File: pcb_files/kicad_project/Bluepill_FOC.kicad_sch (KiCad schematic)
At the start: 27 parts, among them IC1 AS5145B-HSST, J1 Conn_01x03_Pin, J2 Conn_01x03_Pin, SW1 SW_Reset, U4 BluePill, Y2 Crystal

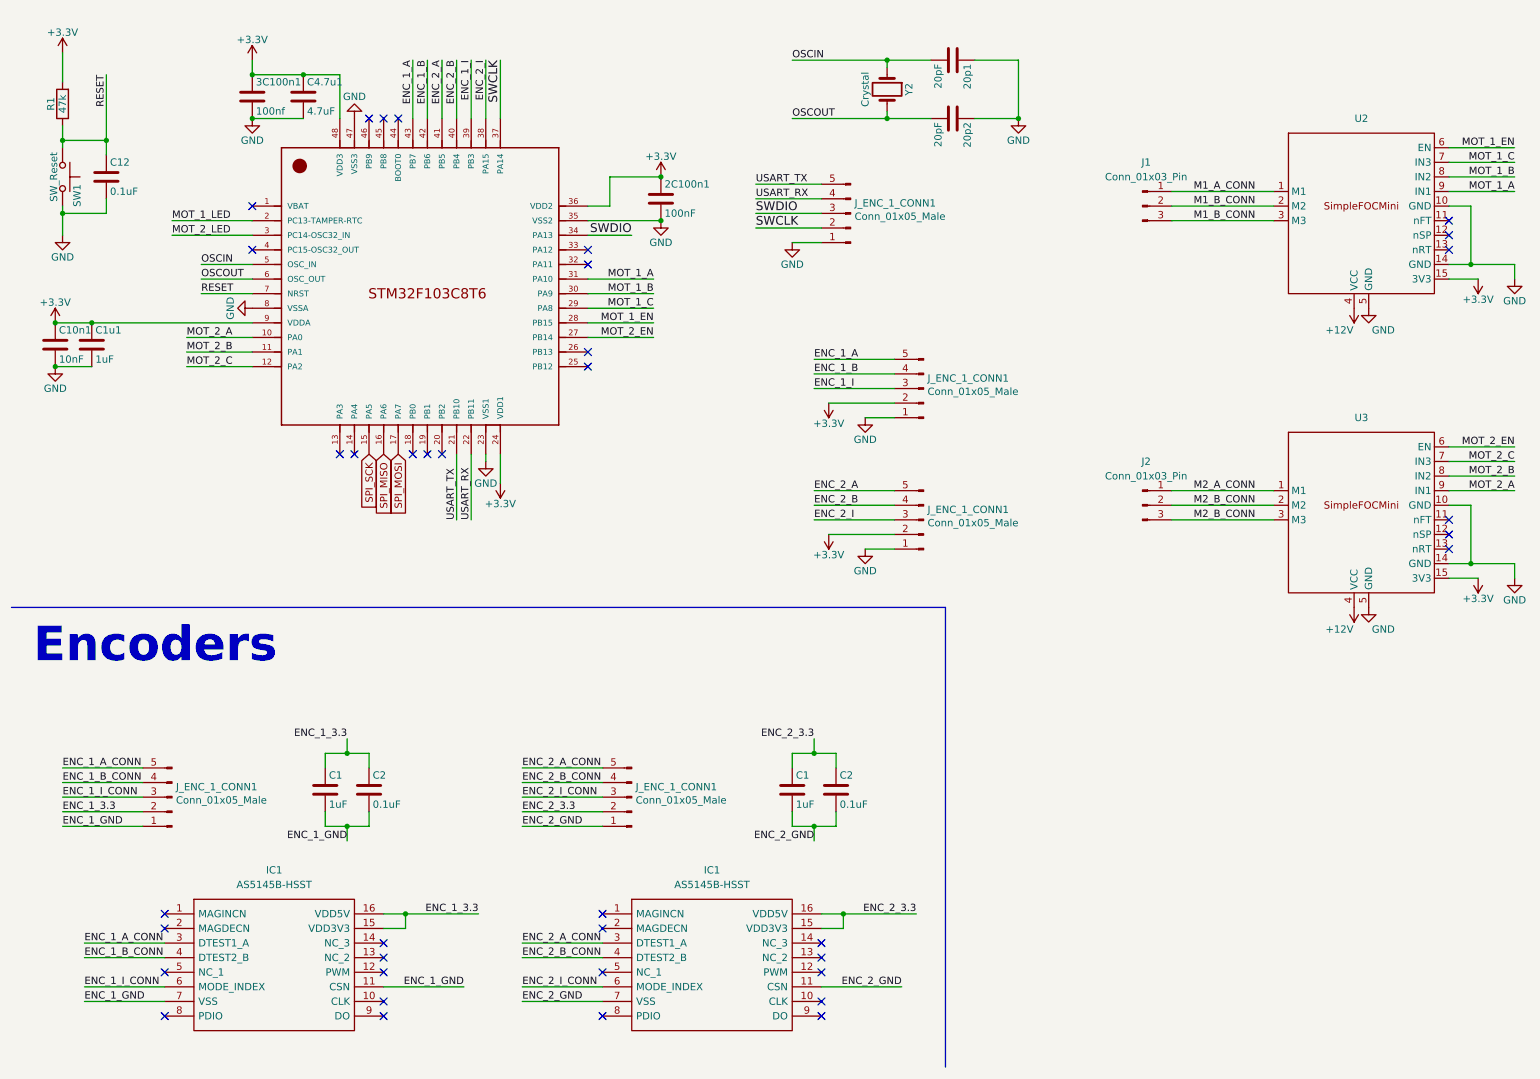
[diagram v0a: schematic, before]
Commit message: Añade pinout de BlackPill, completa esquemático y asocia footprints
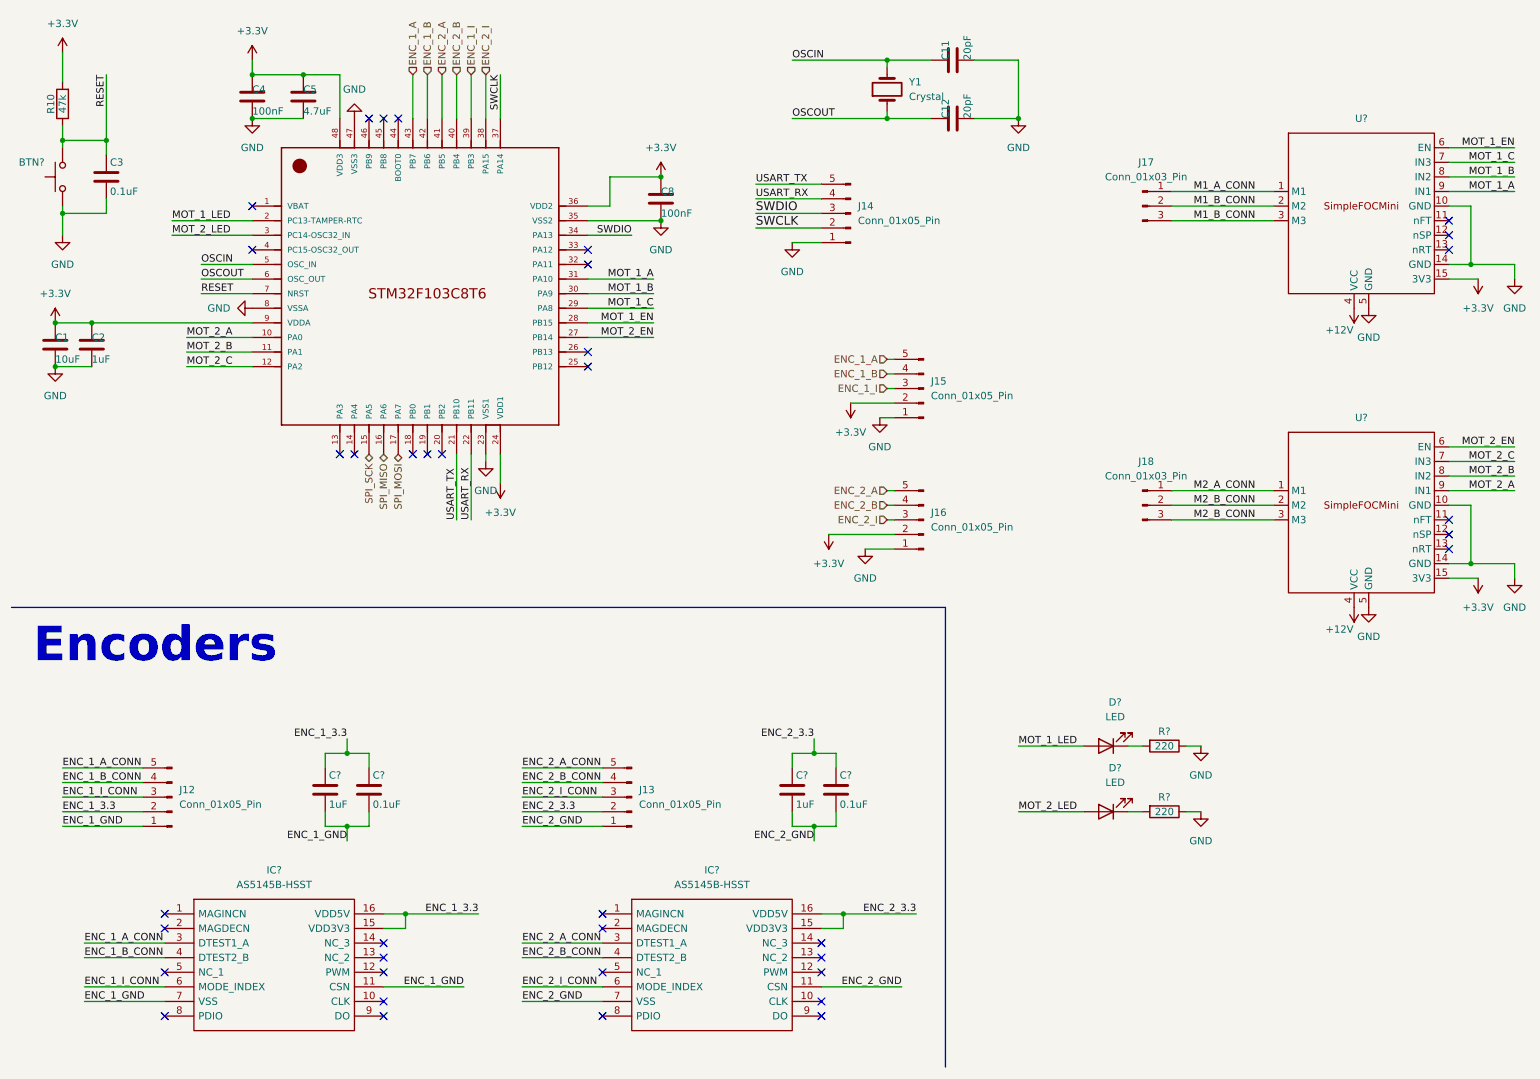
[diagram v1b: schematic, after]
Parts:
- removed 20p1, 20p2: 20pF, Capacitors_SMD:C_0805, symbol DragonBot-rescue:C
- removed 2C100n1: 100nF, Capacitors_SMD:C_0805, symbol DragonBot-rescue:C
- removed 3C100n1: 100nf, Capacitors_SMD:C_0805, symbol DragonBot-rescue:C
- removed C10n1: 10nF, Capacitors_SMD:C_0805, symbol DragonBot-rescue:C
- removed C1u1: 1uF, Capacitors_SMD:C_0805, symbol DragonBot-rescue:C
- removed C4.7u1: 4.7uF, Capacitors_SMD:C_0805, symbol DragonBot-rescue:C
- removed J_ENC_1_CONN1 (x5): Conn_01x05_Male, PCB_ZoroBot_v3:encd_fuji, symbol PCB_ZoroBot_v3-rescue:Conn_01x05_Male-Connector
- removed SW1: SW_Reset, Button_Switch_SMD:SW_SPST_EVQPE1, symbol PCB_ZoroBot_v3-rescue:SW_Push-multiPCB-rescue-multiPCB-rescue-PCB_Fujitora-resc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
- removed Y2: Crystal, Crystals:Crystal_HC50_Vertical, symbol DragonBot-rescue:Crystal
- added BTN?: ~, Button_Switch_SMD:SW_SPST_EVQPE1, symbol custom_libraries:Button
- added C1: 10uF, Capacitor_SMD:C_0805_2012Metric, symbol Device:C
- added C11, C12: 20pF, Capacitor_SMD:C_0805_2012Metric, symbol Device:C
- added C2: 1uF, Capacitor_SMD:C_0805_2012Metric, symbol Device:C
- added C4, C8: 100nF, Capacitor_SMD:C_0805_2012Metric, symbol Device:C
- added C5: 4.7uF, Capacitor_SMD:C_0805_2012Metric, symbol Device:C
- added D? (x2): LED, LED_SMD:LED_0805_2012Metric, symbol Device:LED
- added J12, J13, J14, J15, J16: Conn_01x05_Pin, Connector_PinHeader_2.54mm:PinHeader_1x05_P2.54mm_Vertical, symbol Connector:Conn_01x05_Pin
- added R? (x2): 220, Resistor_SMD:R_0805_2012Metric_Pad1.20x1.40mm_HandSolder, symbol Device:R
- added Y1: Crystal, Crystal:Crystal_SMD_5032-2Pin_5.0x3.2mm, symbol Device:Crystal
- IC? (x2): renamed from IC1; footprint (none) -> Package_SO:SSOP-16_5.3x6.2mm_P0.65mm
- J17: renamed from J1; footprint (none) -> Connector_PinHeader_2.54mm:PinHeader_1x03_P2.54mm_Vertical
- J18: renamed from J2; footprint (none) -> Connector_PinHeader_2.54mm:PinHeader_1x03_P2.54mm_Vertical
- U?: renamed from U4; footprint (none) -> Package_QFP:LQFP-48_7x7mm_P0.5mm
- U?: renamed from U2; footprint (none) -> custom_library:SimpleFOCMini
- U?: renamed from U3; footprint (none) -> custom_library:SimpleFOCMini
- renumbered C12 to C3, C2 to C?, C1 to C?, R1 to R10
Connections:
- net ENC_1_3.3: now also J12.2 (Pin_2)
- net ENC_1_A: now also J15.5 (Pin_5)
- net ENC_1_A_CONN: now also J12.5 (Pin_5)
- net ENC_1_B: now also J15.4 (Pin_4)
- net ENC_1_B_CONN: now also J12.4 (Pin_4)
- net ENC_1_GND: now also J12.1 (Pin_1)
- net ENC_1_I: now also J15.3 (Pin_3)
- net ENC_1_I_CONN: now also J12.3 (Pin_3)
- net ENC_2_3.3: now also J13.2 (Pin_2)
- net ENC_2_A: now also J16.5 (Pin_5)
- net ENC_2_A_CONN: now also J13.5 (Pin_5)
- net ENC_2_B: now also J16.4 (Pin_4)
- net ENC_2_B_CONN: now also J13.4 (Pin_4)
- net ENC_2_GND: now also J13.1 (Pin_1)
- net ENC_2_I: now also J16.3 (Pin_3)
- net ENC_2_I_CONN: now also J13.3 (Pin_3)
- net GND: now also BTN?.1, C1.2, C11.2, C12.2, C2.2, C4.2, C5.2, C8.2, J14.1 (Pin_1), J15.1 (Pin_1), J16.1 (Pin_1), R?.1, R?.1
- net MOT_1_LED: now also D?.2 (A)
- net MOT_2_LED: now also D?.2 (A)
- net OSCIN: now also C11.1, Y1.2
- net OSCOUT: now also C12.1, Y1.1
- net RESET: now also BTN?.2
- net SWCLK: now also J14.2 (Pin_2)
- net SWDIO: now also J14.3 (Pin_3)
- net USART_RX: now also J14.4 (Pin_4)
- net USART_TX: now also J14.5 (Pin_5)
- net +3V3 renamed +3.3V
- net +3.3V: now also C1.1, C2.1, C4.1, C5.1, C8.1, J15.2 (Pin_2), J16.2 (Pin_2)
- new net: D?.1 (K), R?.2 (x2)

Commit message: Actualiza estructura del proyecto (symbols, footprints) y rutas relativas
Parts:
- BTN?: symbol custom_libraries:Button -> custom_symbols:Button
- IC? (x2): symbol custom_libraries:Encoder_AS5145B-HSST -> custom_symbols:Encoder_AS5145B-HSST
- U?: symbol custom_libraries:BluePill -> custom_symbols:BluePill
- U? (x2): footprint custom_library:SimpleFOCMini -> custom_symbols:SimpleFOCMini; symbol custom_libraries:SimpleFOCMini -> custom_symbols:SimpleFOCMini
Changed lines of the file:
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@@
     )
   )
-  (symbol (lib_id "custom_libraries:BluePill") (at 85.09 63.5 0) (unit 1)
+  (symbol (lib_id "custom_symbols:BluePill") (at 85.09 63.5 0) (unit 1)
     (in_bom yes) (on_board yes) (dnp no) (fields_autoplaced)
     (property "Reference" "U?" (at 106.68 36.83 0)
@@
     )
   )
-  (symbol (lib_id "custom_libraries:SimpleFOCMini") (at 247.65 48.26 0) (unit 1)
+  (symbol (lib_id "custom_symbols:SimpleFOCMini") (at 247.65 48.26 0) (unit 1)
     (in_bom yes) (on_board yes) (dnp no) (fields_autoplaced)
     (property "Reference" "U?" (at 247.65 33.02 0)
@@
       (effects (font (size 1.27 1.27)))
     )
-    (property "Footprint" "custom_library:SimpleFOCMini" (at 247.65 48.26 0)
+    (property "Footprint" "custom_symbols:SimpleFOCMini" (at 247.65 48.26 0)
       (effects (font (size 1.27 1.27)) hide)
     )
@@
     )
   )
-  (symbol (lib_id "custom_libraries:SimpleFOCMini") (at 247.65 100.33 0) (unit 1)
+  (symbol (lib_id "custom_symbols:SimpleFOCMini") (at 247.65 100.33 0) (unit 1)
     (in_bom yes) (on_board yes) (dnp no) (fields_autoplaced)
     (property "Reference" "U?" (at 247.65 85.09 0)
@@
       (effects (font (size 1.27 1.27)))
     )
-    (property "Footprint" "custom_library:SimpleFOCMini" (at 247.65 100.33 0)
+    (property "Footprint" "custom_symbols:SimpleFOCMini" (at 247.65 100.33 0)
       (effects (font (size 1.27 1.27)) hide)
     )
@@
     )
   )
-  (symbol (lib_id "custom_libraries:Button") (at 21.59 43.18 90) (unit 1)
+  (symbol (lib_id "custom_symbols:Button") (at 21.59 43.18 90) (unit 1)
     (in_bom yes) (on_board yes) (dnp no)
     (property "Reference" "BTN?" (at 13.97 40.64 90)
@@
     )
   )
-  (symbol (lib_id "custom_libraries:Encoder_AS5145B-HSST") (at 115.57 171.45 0) (unit 1)
+  (symbol (lib_id "custom_symbols:Encoder_AS5145B-HSST") (at 115.57 171.45 0) (unit 1)
     (in_bom yes) (on_board yes) (dnp no) (fields_autoplaced)
     (property "Reference" "IC?" (at 134.62 163.83 0)
@@
     )
   )
-  (symbol (lib_id "custom_libraries:Encoder_AS5145B-HSST") (at 39.37 171.45 0) (unit 1)
+  (symbol (lib_id "custom_symbols:Encoder_AS5145B-HSST") (at 39.37 171.45 0) (unit 1)
     (in_bom yes) (on_board yes) (dnp no) (fields_autoplaced)
     (property "Reference" "IC?" (at 58.42 163.83 0)

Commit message: Actualiza el esquemático de la PCB
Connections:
- net SPI_NSS: now reaches U?.14 (PA4)
- net USART_RX renamed USART3_RX
- net USART3_RX: now also U?.21 (PB10); no longer U?.22 (PB11)
- net USART_TX renamed USART3_TX
- net USART3_TX: now also U?.22 (PB11); no longer U?.21 (PB10)
- no-connect marks 38 -> 37
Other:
- moved on the sheet: J14
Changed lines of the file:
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@@
   (no_connect (at 54.61 48.26))
   (no_connect (at 262.89 102.87))
-  (no_connect (at 72.39 91.44))
   (no_connect (at 74.93 33.02))
   (no_connect (at 153.67 189.23))
@@
     (stroke (width 0) (type default))
   )
-  (wire (pts (xy 142.24 46.99) (xy 153.67 46.99))
-    (stroke (width 0) (type default))
-  )
   (wire (pts (xy 262.89 38.1) (xy 274.32 38.1))
     (stroke (width 0) (type default))
@@
     (stroke (width 0) (type default))
   )
-  (wire (pts (xy 148.59 54.61) (xy 153.67 54.61))
+  (wire (pts (xy 154.94 57.15) (xy 160.02 57.15))
     (stroke (width 0) (type default))
   )
@@
   )
   (wire (pts (xy 77.47 171.45) (xy 81.28 171.45))
-    (stroke (width 0) (type default))
-  )
-  (wire (pts (xy 90.17 91.44) (xy 90.17 102.87))
     (stroke (width 0) (type default))
   )
@@
     (stroke (width 0) (type default))
   )
-  (wire (pts (xy 142.24 44.45) (xy 153.67 44.45))
-    (stroke (width 0) (type default))
-  )
   (wire (pts (xy 214.63 45.72) (xy 232.41 45.72))
     (stroke (width 0) (type default))
@@
     (stroke (width 0) (type default))
   )
-  (wire (pts (xy 142.24 52.07) (xy 153.67 52.07))
+  (wire (pts (xy 139.7 54.61) (xy 160.02 54.61))
     (stroke (width 0) (type default))
   )
@@
     (stroke (width 0) (type default))
   )
-  (wire (pts (xy 92.71 91.44) (xy 92.71 102.87))
-    (stroke (width 0) (type default))
-  )
   (wire (pts (xy 153.67 173.99) (xy 157.48 173.99))
     (stroke (width 0) (type default))
@@
     (stroke (width 0) (type default))
   )
-  (wire (pts (xy 142.24 49.53) (xy 153.67 49.53))
+  (wire (pts (xy 139.7 52.07) (xy 160.02 52.07))
     (stroke (width 0) (type default))
   )
@@
     (effects (font (size 1.27 1.27)) (justify left bottom))
   )
-  (label "USART_RX" (at 92.71 102.87 90) (fields_autoplaced)
-    (effects (font (size 1.27 1.27)) (justify left bottom))
-  )
   (label "MOT_1_LED" (at 187.96 142.24 0) (fields_autoplaced)
     (effects (font (size 1.27 1.27)) (justify left bottom))
@@
     (effects (font (size 1.27 1.27)) (justify left bottom))
   )
-  (label "USART_TX" (at 142.24 44.45 0) (fields_autoplaced)
-    (effects (font (size 1.27 1.27)) (justify left bottom))
-  )
   (label "OSCOUT" (at 45.72 60.96 0) (fields_autoplaced)
     (effects (font (size 1.27 1.27)) (justify left bottom))
@@
     (effects (font (size 1.27 1.27)) (justify left bottom))
   )
-  (label "USART_TX" (at 90.17 102.87 90) (fields_autoplaced)
-    (effects (font (size 1.27 1.27)) (justify left bottom))
-  )
   (label "SWDIO" (at 120.65 53.34 180) (fields_autoplaced)
     (effects (font (size 1.27 1.27)) (justify right bottom))
@@
     (effects (font (size 1.27 1.27)) (justify left bottom))
   )
-  (label "SWDIO" (at 142.24 49.53 0) (fields_autoplaced)
+  (label "SWDIO" (at 139.7 52.07 0) (fields_autoplaced)
     (effects (font (size 1.524 1.524)) (justify left bottom))
   )
@@
     (effects (font (size 1.27 1.27)) (justify left bottom))
   )
-  (label "SWCLK" (at 142.24 52.07 0) (fields_autoplaced)
+  (label "SWCLK" (at 139.7 54.61 0) (fields_autoplaced)
     (effects (font (size 1.524 1.524)) (justify left bottom))
   )
@@
   (label "SWCLK" (at 97.79 25.4 270) (fields_autoplaced)
     (effects (font (size 1.27 1.27)) (justify right bottom))
-  )
-  (label "USART_RX" (at 142.24 46.99 0) (fields_autoplaced)
-    (effects (font (size 1.27 1.27)) (justify left bottom))
   )
   (label "MOT_1_LED" (at 40.64 50.8 0) (fields_autoplaced)
@@
     (effects (font (size 1.27 1.27)) (justify left))
   )
+  (hierarchical_label "USART3_TX" (shape input) (at 160.02 46.99 180) (fields_autoplaced)
+    (effects (font (size 1.27 1.27)) (justify right))
+  )
+  (hierarchical_label "USART3_TX" (shape input) (at 92.71 91.44 270) (fields_autoplaced)
+    (effects (font (size 1.27 1.27)) (justify right))
+  )
   (hierarchical_label "SPI_MOSI" (shape bidirectional) (at 80.01 91.44 270) (fields_autoplaced)
     (effects (font (size 1.27 1.27)) (justify right))
@@
     (effects (font (size 1.27 1.27)) (justify right))
   )
+  (hierarchical_label "SPI_NSS" (shape bidirectional) (at 72.39 91.44 270) (fields_autoplaced)
+    (effects (font (size 1.27 1.27)) (justify right))
+  )
   (hierarchical_label "ENC_2_B" (shape input) (at 90.17 25.4 90) (fields_autoplaced)
     (effects (font (size 1.27 1.27)) (justify left))
@@
   (hierarchical_label "ENC_1_A" (shape input) (at 82.55 25.4 90) (fields_autoplaced)
     (effects (font (size 1.27 1.27)) (justify left))
+  )
+  (hierarchical_label "USART3_RX" (shape input) (at 90.17 91.44 270) (fields_autoplaced)
+    (effects (font (size 1.27 1.27)) (justify right))
+  )
+  (hierarchical_label "USART3_RX" (shape input) (at 160.02 49.53 180) (fields_autoplaced)
+    (effects (font (size 1.27 1.27)) (justify right))
   )
   (hierarchical_label "ENC_1_I" (shape input) (at 92.71 25.4 90) (fields_autoplaced)
@@
     )
   )
-  (symbol (lib_id "power:GND") (at 148.59 54.61 0) (unit 1)
-    (in_bom yes) (on_board yes) (dnp no) (fields_autoplaced)
-    (property "Reference" "#PWR055" (at 148.59 60.96 0)
-      (effects (font (size 1.27 1.27)) hide)
-    )
-    (property "Value" "GND" (at 148.59 59.69 0)
-      (effects (font (size 1.27 1.27)))
-    )
-    (property "Footprint" "" (at 148.59 54.61 0)
-      (effects (font (size 1.27 1.27)) hide)
-    )
-    (property "Datasheet" "" (at 148.59 54.61 0)
+  (symbol (lib_id "power:GND") (at 154.94 57.15 0) (unit 1)
+    (in_bom yes) (on_board yes) (dnp no) (fields_autoplaced)
+    (property "Reference" "#PWR055" (at 154.94 63.5 0)
+      (effects (font (size 1.27 1.27)) hide)
+    )
+    (property "Value" "GND" (at 154.94 62.23 0)
+      (effects (font (size 1.27 1.27)))
+    )
+    (property "Footprint" "" (at 154.94 57.15 0)
+      (effects (font (size 1.27 1.27)) hide)
+    )
+    (property "Datasheet" "" (at 154.94 57.15 0)
       (effects (font (size 1.27 1.27)) hide)
     )
@@
     )
   )
-  (symbol (lib_id "Connector:Conn_01x05_Pin") (at 158.75 49.53 180) (unit 1)
-    (in_bom yes) (on_board yes) (dnp no) (fields_autoplaced)
-    (property "Reference" "J14" (at 160.02 48.26 0)
+  (symbol (lib_id "Connector:Conn_01x05_Pin") (at 165.1 52.07 180) (unit 1)
+    (in_bom yes) (on_board yes) (dnp no) (fields_autoplaced)
+    (property "Reference" "J14" (at 166.37 50.8 0)
       (effects (font (size 1.27 1.27)) (justify right))
     )
-    (property "Value" "Conn_01x05_Pin" (at 160.02 50.8 0)
+    (property "Value" "Conn_01x05_Pin" (at 166.37 53.34 0)
       (effects (font (size 1.27 1.27)) (justify right))
     )
-    (property "Footprint" "Connector_PinHeader_2.54mm:PinHeader_1x05_P2.54mm_Vertical" (at 158.75 49.53 0)
-      (effects (font (size 1.27 1.27)) hide)
-    )
-    (property "Datasheet" "~" (at 158.75 49.53 0)
-      (effects (font (size 1.27 1.27)) hide)
-    )
+    (property "Footprint" "Connector_PinHeader_2.54mm:PinHeader_1x05_P2.54mm_Vertical" (at 165.1 52.07 0)
+      (effects (font (size 1.27 1.27)) hide)
+    )
+    (property "Datasheet" "~" (at 165.1 52.07 0)
+      (effects (font (size 1.27 1.27)) hide)
+    )
